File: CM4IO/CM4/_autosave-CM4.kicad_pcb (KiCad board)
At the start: 4 copper layers, 113 parts, among them IC1 OPA659IDBVR, IC2 OPA659IDBVR, IC3 LMH6643MAX_NOPB, IC4 TPS65133DPDR, IC5 TPS62111RSAT, IC6 STM32H747IIT6, J1 901-144-8RFX, J2 USB_C_Receptacle_USB2.0, J3 SWDIO, J4 Micro_SD_Card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

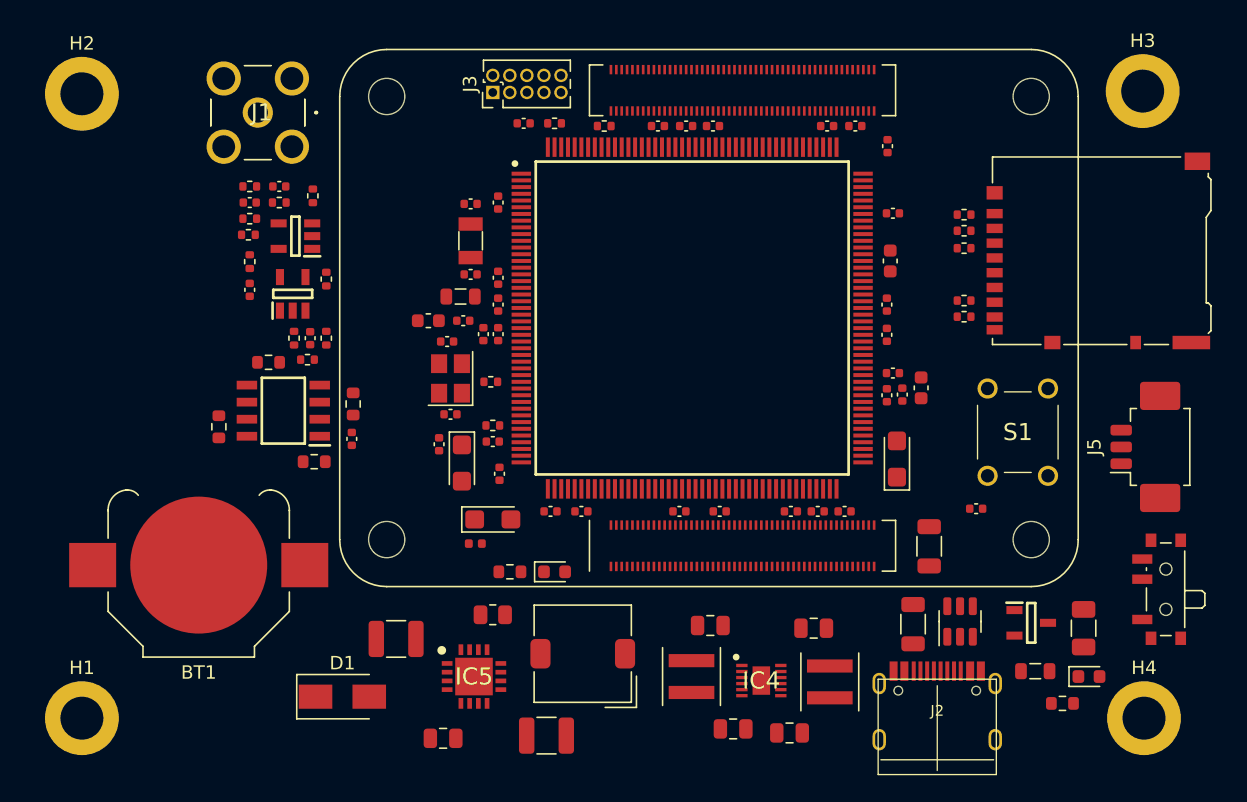
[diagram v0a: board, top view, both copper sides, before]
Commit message: Initial CM4IO board design
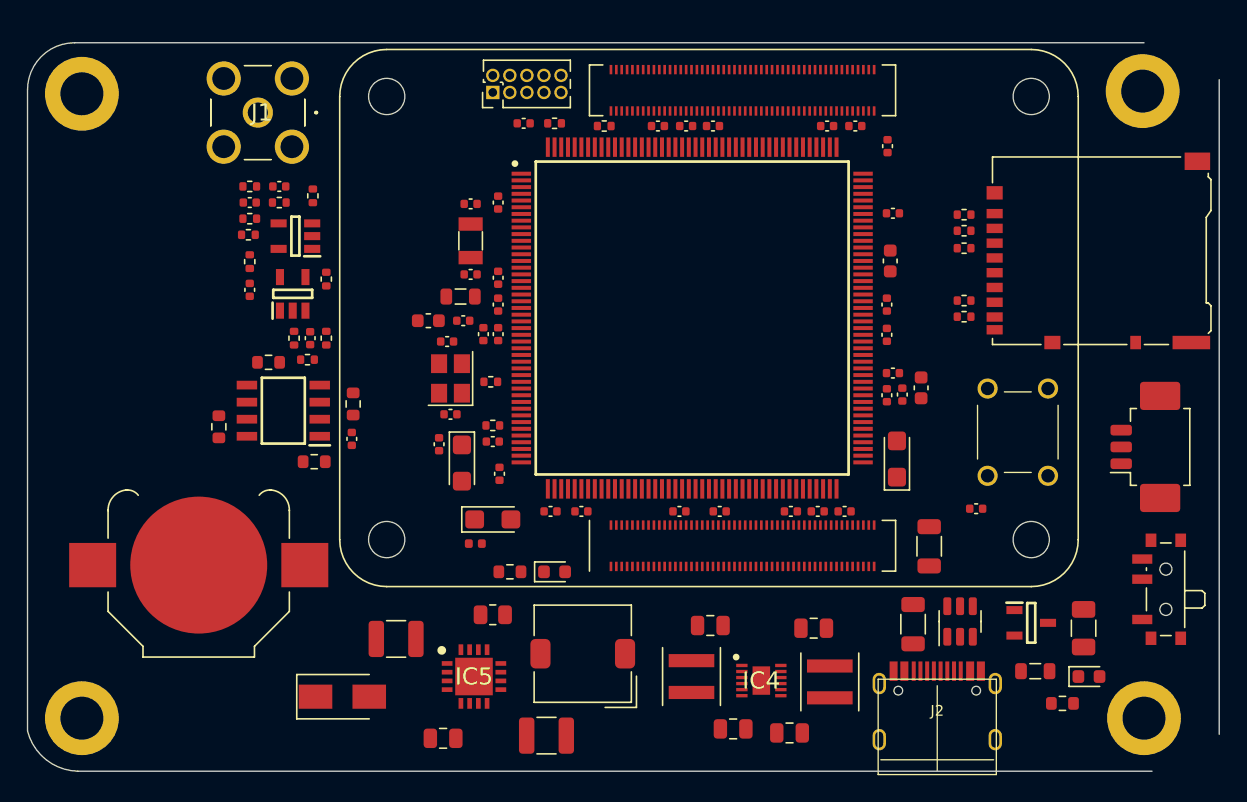
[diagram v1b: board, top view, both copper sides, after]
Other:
- board outline added: 88.8 x 54.2 mm
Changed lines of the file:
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@@
     (property "Sheet name" "H7MCU")
     (attr through_hole)
-    (fp_text reference "J3" (at 0.635 -1.695 90) (layer "F.SilkS")
+    (fp_text reference "J3" (at 0.635 -1.695 90) (layer "F.SilkS") hide
       (effects (font (size 1 1) (thickness 0.15)))
     )
@@
     (property "Sheet name" "H7MCU")
     (attr smd)
-    (fp_text reference "D1" (at 0 -2.5) (layer "F.SilkS")
+    (fp_text reference "D1" (at 0 -2.5) (layer "F.SilkS") hide
       (effects (font (size 1 1) (thickness 0.15)))
     )
@@
     (property "Sheet name" "")
     (attr exclude_from_pos_files)
-    (fp_text reference "H3" (at 0 -3.75) (layer "F.SilkS")
+    (fp_text reference "H3" (at 0 -3.75) (layer "F.SilkS") hide
       (effects (font (size 1 1) (thickness 0.15)))
     )
@@
     (property "Sheet name" "")
     (attr exclude_from_pos_files)
-    (fp_text reference "H2" (at 0 -3.75) (layer "F.SilkS")
+    (fp_text reference "H2" (at 0 -3.75) (layer "F.SilkS") hide
       (effects (font (size 1 1) (thickness 0.15)))
     )
@@
     (property "Sheet name" "")
     (attr exclude_from_pos_files)
-    (fp_text reference "H4" (at 0 -3.75) (layer "F.SilkS")
+    (fp_text reference "H4" (at 0 -3.75) (layer "F.SilkS") hide
       (effects (font (size 1 1) (thickness 0.15)))
     )
@@
     (property "Sheet name" "H7MCU")
     (attr smd)
-    (fp_text reference "BT1" (at 0 -8) (layer "F.SilkS")
+    (fp_text reference "BT1" (at 0 -8) (layer "F.SilkS") hide
       (effects (font (size 1 1) (thickness 0.15)))
     )
@@
     (property "Sheet name" "CM4_GPIO")
     (attr smd)
-    (fp_text reference "J5" (at 0 -4.4 90) (layer "F.SilkS")
+    (fp_text reference "J5" (at 0 -4.4 90) (layer "F.SilkS") hide
       (effects (font (size 1 1) (thickness 0.15)))
     )
@@
     (property "Sheet name" "H7MCU")
     (attr through_hole)
-    (fp_text reference "S1" (at 0 0 180) (layer "F.SilkS")
+    (fp_text reference "S1" (at 0 0 180) (layer "F.SilkS") hide
       (effects (font (size 1.27 1.27) (thickness 0.254)))
     )
@@
     (property "Sheet name" "")
     (attr exclude_from_pos_files)
-    (fp_text reference "H1" (at 0 -3.75) (layer "F.SilkS")
+    (fp_text reference "H1" (at 0 -3.75) (layer "F.SilkS") hide
       (effects (font (size 1 1) (thickness 0.15)))
     )
@@
     )
   )
+  (gr_line (start 65.75 82) (end 145.4 82) (layer "Edge.Cuts") (width 0.1))
+  (gr_arc (start 66.093774 132.289033) (end 62.250001 133.249999) (angle -74.60724052) (layer "Edge.Cuts") (width 0.1))
+  (gr_line (start 62.25 133.25) (end 62.25 85.5) (layer "Edge.Cuts") (width 0.1))
+  (gr_line (start 151 84.75) (end 151 133.5) (layer "Edge.Cuts") (width 0.1))
+  (gr_line (start 146 136.25) (end 66 136.25) (layer "Edge.Cuts") (width 0.1))
+  (gr_arc (start 65.75 85.5) (end 62.25 85.5) (angle 90) (layer "Edge.Cuts") (width 0.1))
 )
